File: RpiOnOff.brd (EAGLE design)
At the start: 38 x 11.1 mm, 22 parts, among them CON1 CONNECTOR-1X2[2.54MM], CON2 CONNECTOR-1X2[2.54MM], Q1 BSS84, Q2 BSS123

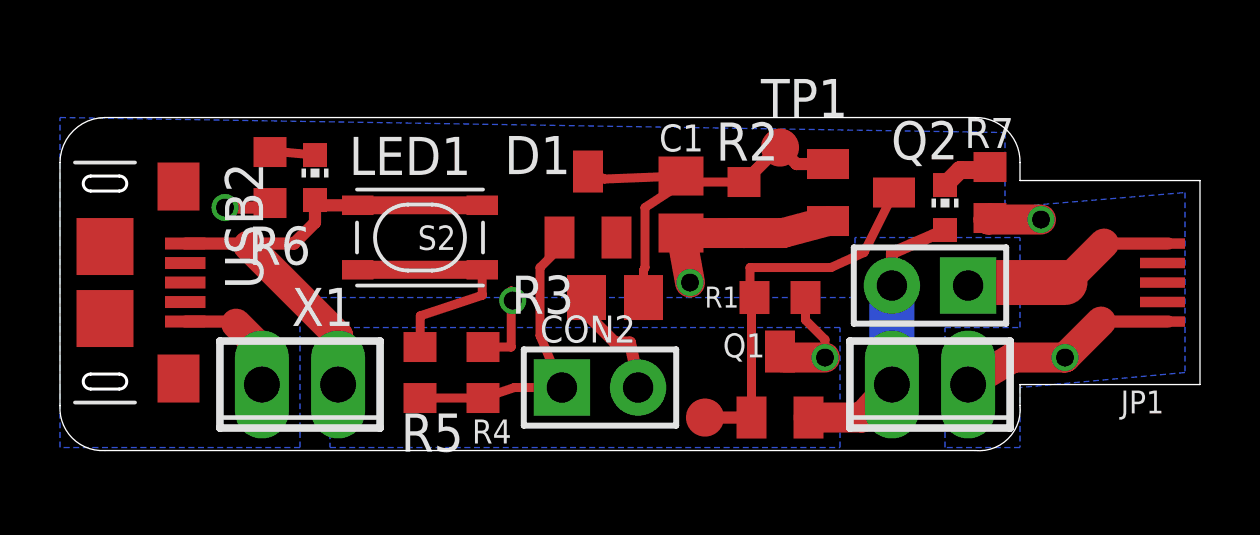
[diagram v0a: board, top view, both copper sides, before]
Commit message: I think the main change was fixing a transistor footprint.
This is the version that was sent for production to Seeed Studios.
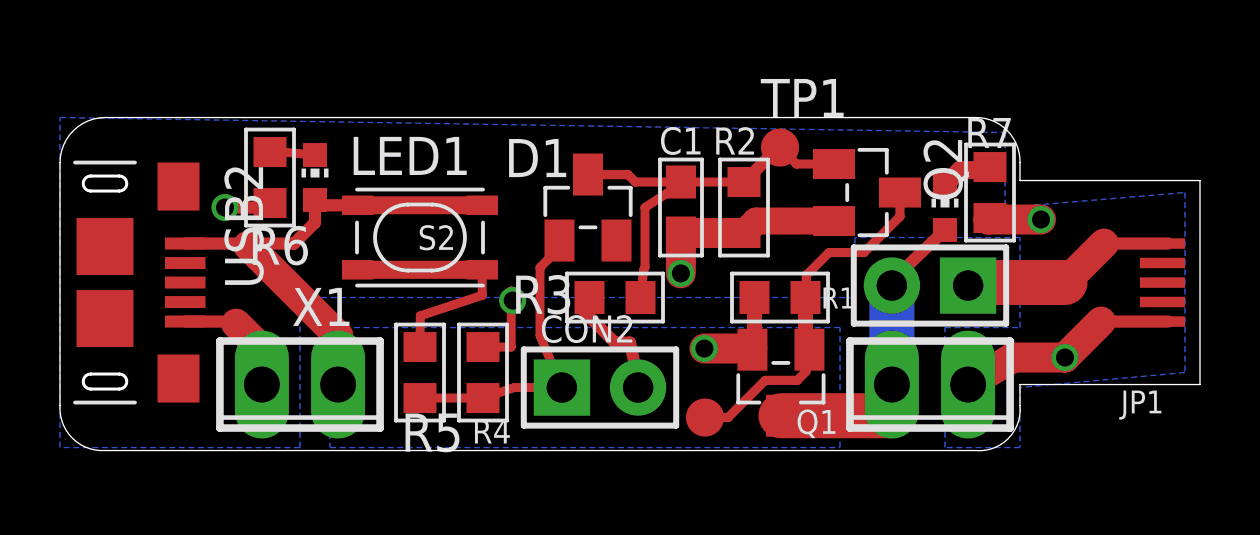
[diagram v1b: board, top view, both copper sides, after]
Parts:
- C1: device rcl:C0805 -> Erland's Library:C0603
- Q1: value BSS84 -> MOSFET-P-TOSHIBA-SSM3J338R; device transistor-small-signal:SOT23 -> Erland's Library:SOT23
- Q2: value BSS123 -> MOSFET-N-SSM3K36MFV; device transistor-small-signal:SOT23 -> Erland's Library:SOT23
- R1, R2, R4, R5, R6, R7: device rcl:R0603 -> Erland's Library:R0603
- R3: device rcl:R0805 -> Erland's Library:R0603
- moved Q2 0.20 mm to (22.9, 5.50)
- moved C1 0.10 mm to (16.7, 5.00)
- moved D1 0.10 mm to (13.6, 5.00)
- moved Q1 0.07 mm to (20.0, -0.84), turned to 180 degrees
- turned R1 to 0 degrees
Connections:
- net +5V: now also Q1.2; no longer Q1.3
- net VDD: now also Q1.3; no longer Q1.2
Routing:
- net VDD: track 9.58 -> 10.6 mm
- net Q1GATE: track 12.8 -> 12.1 mm
